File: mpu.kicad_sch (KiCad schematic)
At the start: 31 parts, among them SW501 SW_DIP_x03, U501 STM32MP135FAE7, Y501 32.768 kHz, Y502 24 MHz

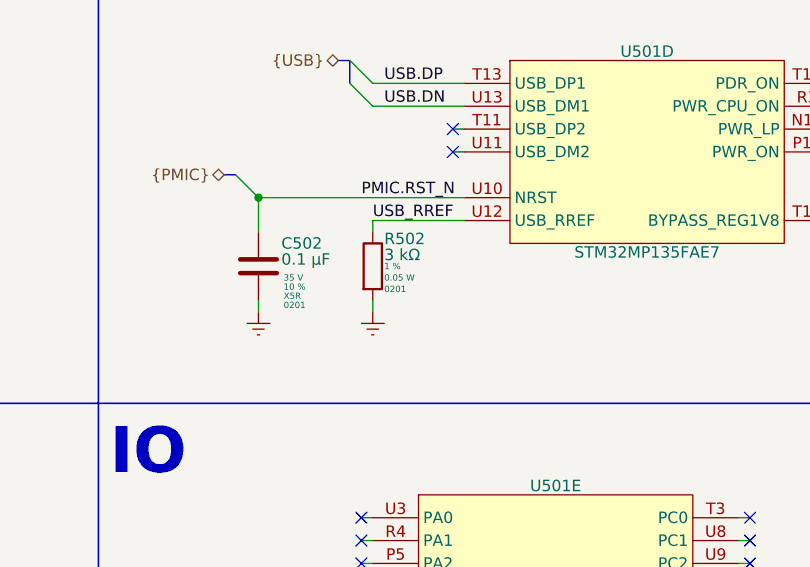
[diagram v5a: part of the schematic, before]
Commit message: Refactor BOM
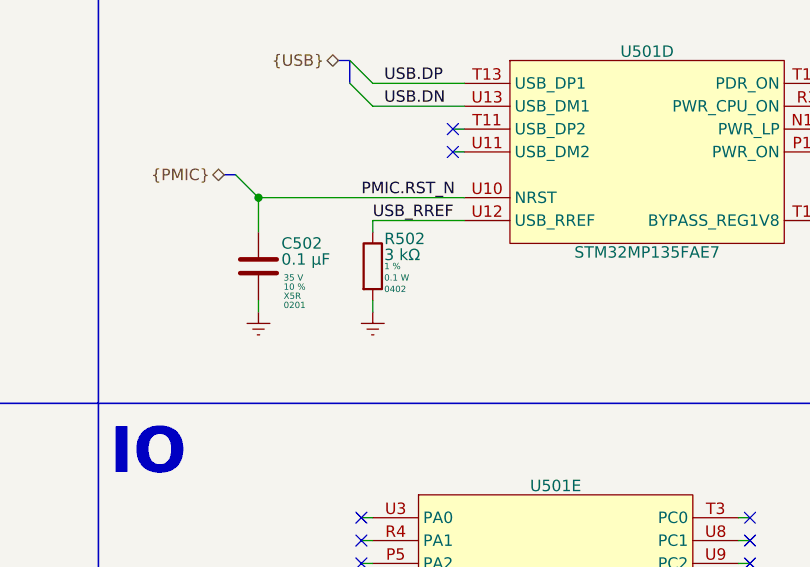
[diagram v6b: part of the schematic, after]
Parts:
- R502: footprint perfect_footprints:R_0201_0603Metric -> perfect_footprints:R_0402_1005Metric; Digi-Key Part Number P122912CT-ND -> 738-RNCF0402DTE3K00CT-ND; MPN ERJ-1GNF3001C -> RNCF0402DTE3K00; Power rating 0.05 W -> 0.1 W; Size 0201 -> 0402
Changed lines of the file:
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@@
 	)
 	(symbol
+		(lib_id "Device:R")
+		(at 157.48 99.06 0)
+		(unit 1)
+		(exclude_from_sim no)
+		(in_bom yes)
+		(on_board yes)
+		(dnp no)
+		(property "Reference" "R502"
+			(at 158.75 96.012 0)
+			(effects
+				(font
+					(size 1.27 1.27)
+				)
+				(justify left)
+			)
+		)
+		(property "Value" "3 kΩ"
+			(at 158.75 97.79 0)
+			(effects
+				(font
+					(size 1.27 1.27)
+				)
+				(justify left)
+			)
+		)
+		(property "Footprint" "perfect_footprints:R_0402_1005Metric"
+			(at 155.702 99.06 90)
+			(effects
+				(font
+					(size 1.27 1.27)
+				)
+				(hide yes)
+			)
+		)
+		(property "Datasheet" "https://www.seielect.com/catalog/SEI-RNCF.pdf"
+			(at 157.48 99.06 0)
+			(effects
+				(font
+					(size 1.27 1.27)
+				)
+				(hide yes)
+			)
+		)
+		(property "Description" "3 kOhms ±0.5% 0.1W, 1/10W Chip Resistor 0402 (1005 Metric) Automotive AEC-Q200 Thin Film"
+			(at 157.48 99.06 0)
+			(effects
+				(font
+					(size 1.27 1.27)
+				)
+				(hide yes)
+			)
+		)
+		(property "MPN" "RNCF0402DTE3K00"
+			(at 157.48 99.06 0)
+			(effects
+				(font
+					(size 1.27 1.27)
+				)
+				(hide yes)
+			)
+		)
+		(property "Manufacturer" "Stackpole Electronics Inc"
+			(at 157.48 99.06 0)
+			(effects
+				(font
+					(size 1.27 1.27)
+				)
+				(hide yes)
+			)
+		)
+		(property "Tolerance" "1 %"
+			(at 158.75 99.06 0)
+			(effects
+				(font
+					(size 0.7 0.7)
+				)
+				(justify left)
+			)
+		)
+		(property "Power rating" "0.1 W"
+			(at 158.75 100.33 0)
+			(effects
+				(font
+					(size 0.7 0.7)
+				)
+				(justify left)
+			)
+		)
+		(property "Size" "0402"
+			(at 158.75 101.6001 0)
+			(effects
+				(font
+					(size 0.7 0.7)
+				)
+				(justify left)
+			)
+		)
+		(property "Digi-Key Part Number" "738-RNCF0402DTE3K00CT-ND"
+			(at 157.48 99.06 0)
+			(effects
+				(font
+					(size 1.27 1.27)
+				)
+				(hide yes)
+			)
+		)
+		(pin "2"
+		)
+		(pin "1"
+		)
+		(instances
+			(project "linux-sbc"
+				(path "/fa11a02f-8043-4153-ab69-88d766503017/2d01087b-54dc-4f43-9cc7-a0ba17201776"
+					(reference "R502")
+					(unit 1)
+				)
+			)
+		)
+	)
+	(symbol
 		(lib_name "LED_1")
 		(lib_id "Device:LED")
@@
 					(unit 1)
 				)
-			)
-		)
-	)
-	(symbol
-		(lib_id "Device:R")
-		(at 157.48 99.06 0)
-		(unit 1)
-		(exclude_from_sim no)
-		(in_bom yes)
-		(on_board yes)
-		(dnp no)
-		(property "Reference" "R502"
-			(at 158.75 96.012 0)
-			(effects
-				(font
-					(size 1.27 1.27)
-				)
-				(justify left)
-			)
-		)
-		(property "Value" "3 kΩ"
-			(at 158.75 97.79 0)
-			(effects
-				(font
-					(size 1.27 1.27)
-				)
-				(justify left)
-			)
-		)
-		(property "Footprint" "perfect_footprints:R_0201_0603Metric"
-			(at 155.702 99.06 90)
-			(effects
-				(font
-					(size 1.27 1.27)
-				)
-				(hide yes)
-			)
-		)
-		(property "Datasheet" "https://industrial.panasonic.com/cdbs/www-data/pdf/RDA0000/AOA0000C304.pdf"
-			(at 157.48 99.06 0)
-			(effects
-				(font
-					(size 1.27 1.27)
-				)
-				(hide yes)
-			)
-		)
-		(property "Description" "3 kOhms ±1% 0.05W, 1/20W Chip Resistor 0201 (0603 Metric) Thick Film"
-			(at 157.48 99.06 0)
-			(effects
-				(font
-					(size 1.27 1.27)
-				)
-				(hide yes)
-			)
-		)
-		(property "MPN" "ERJ-1GNF3001C"
-			(at 157.48 99.06 0)
-			(effects
-				(font
-					(size 1.27 1.27)
-				)
-				(hide yes)
-			)
-		)
-		(property "Manufacturer" "Stackpole Electronics Inc"
-			(at 157.48 99.06 0)
-			(effects
-				(font
-					(size 1.27 1.27)
-				)
-				(hide yes)
-			)
-		)
-		(property "Tolerance" "1 %"
-			(at 158.75 99.06 0)
-			(effects
-				(font
-					(size 0.7 0.7)
-				)
-				(justify left)
-			)
-		)
-		(property "Power rating" "0.05 W"
-			(at 158.75 100.33 0)
-			(effects
-				(font
-					(size 0.7 0.7)
-				)
-				(justify left)
-			)
-		)
-		(property "Size" "0201"
-			(at 158.75 101.6001 0)
-			(effects
-				(font
-					(size 0.7 0.7)
-				)
-				(justify left)
-			)
-		)
-		(property "Digi-Key Part Number" "P122912CT-ND"
-			(at 157.48 99.06 0)
-			(effects
-				(font
-					(size 1.27 1.27)
-				)
-				(hide yes)
-			)
-		)
-		(pin "2"
-		)
-		(pin "1"
-		)
-		(instances
-			(project "linux-sbc"
-				(path "/fa11a02f-8043-4153-ab69-88d766503017/2d01087b-54dc-4f43-9cc7-a0ba17201776"
-					(reference "R502")
-					(unit 1)
-				)

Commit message: Clean up schematics
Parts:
- D501, D502, R505, R506: now not fitted; now left out of the parts list
- SW501: value SW_DIP_x03 -> 3x DIP switch
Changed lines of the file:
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@@
 	(title_block
 		(title "Linux SBC")
-		(date "2025-12-19")
+		(date "2025-12-26")
 		(rev "v1.0.0")
 	)
@@
 			)
 		)
-		(property "Value" "SW_DIP_x03"
+		(property "Value" "3x DIP switch"
 			(at 392.43 108.204 0)
 			(effects
@@
 		(unit 1)
 		(exclude_from_sim no)
-		(in_bom yes)
+		(in_bom no)
 		(on_board yes)
-		(dnp no)
+		(dnp yes)
 		(property "Reference" "R506"
 			(at 323.85 236.474 90)
@@
 		(unit 1)
 		(exclude_from_sim no)
-		(in_bom yes)
+		(in_bom no)
 		(on_board yes)
-		(dnp no)
+		(dnp yes)
 		(property "Reference" "D501"
 			(at 313.69 234.188 0)
@@
 		(unit 1)
 		(exclude_from_sim no)
-		(in_bom yes)
+		(in_bom no)
 		(on_board yes)
-		(dnp no)
+		(dnp yes)
 		(property "Reference" "R505"
 			(at 323.85 226.314 90)
@@
 		(unit 1)
 		(exclude_from_sim no)
-		(in_bom yes)
+		(in_bom no)
 		(on_board yes)
-		(dnp no)
+		(dnp yes)
 		(property "Reference" "D502"
 			(at 313.69 244.348 0)

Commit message: MPU: Use SMD DIP switch
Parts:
- SW501: footprint Button_Switch_THT:SW_DIP_SPSTx03_Slide_9.78x9.8mm_W7.62mm_P2.54mm -> Button_Switch_SMD:SW_DIP_SPSTx03_Slide_6.7x9.18mm_W8.61mm_P2.54mm_LowProfile; Digi-Key Part Number 2223-DS01C-254-S-03BE-ND -> CT2193MST-ND; MPN DS01C-254-S-03BE -> 219-3MST; Manufacturer Same Sky (Formerly CUI Devices) -> CTS Electrocomponents
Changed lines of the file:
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@@
 			)
 		)
-		(property "Footprint" "Button_Switch_THT:SW_DIP_SPSTx03_Slide_9.78x9.8mm_W7.62mm_P2.54mm"
+		(property "Footprint" "Button_Switch_SMD:SW_DIP_SPSTx03_Slide_6.7x9.18mm_W8.61mm_P2.54mm_LowProfile"
 			(at 392.43 105.41 0)
 			(effects
@@
 			)
 		)
-		(property "Datasheet" "https://www.cuidevices.com/product/resource/ds01-254.pdf"
+		(property "Datasheet" "https://www.ctscorp.com/Files/DataSheets/Switches/DIP-Switches/CTS-Switches-DIP-219-Series-Datasheet.pdf"
 			(at 392.43 105.41 0)
 			(effects
@@
 			)
 		)
-		(property "Description" "3x DIP Switch, Single Pole Single Throw (SPST) switch, small symbol"
+		(property "Description" "Dip Switch SPST 3 Position Surface Mount Slide (Standard) Actuator 100mA 20VDC"
 			(at 392.43 102.87 0)
 			(effects
@@
 			)
 		)
-		(property "Digi-Key Part Number" "2223-DS01C-254-S-03BE-ND"
+		(property "Digi-Key Part Number" "CT2193MST-ND"
 			(at 392.43 102.87 0)
 			(effects
@@
 			)
 		)
-		(property "MPN" "DS01C-254-S-03BE"
+		(property "MPN" "219-3MST"
 			(at 392.43 102.87 0)
 			(effects
@@
 			)
 		)
-		(property "Manufacturer" "Same Sky (Formerly CUI Devices)"
+		(property "Manufacturer" "CTS Electrocomponents"
 			(at 392.43 102.87 0)
 			(effects
